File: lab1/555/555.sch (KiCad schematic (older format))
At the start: 8 parts, among them IC1 MC9S08QG8xPBE, U1 LM555

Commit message: actualizacion esquematico correccion tierra en LED-RGB e imagenes para el informe
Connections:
- net +5V: now also Rc.1
- net GND: no longer Rc.2
- net at D1.1 (A): now also Rc.2; no longer Rc.1
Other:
- moved on the sheet: Rc
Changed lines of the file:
@@
 $EndComp
-$Comp
-L power:GND #PWR?
-U 1 1 5EB46ACA
-P 6350 2050
-F 0 "#PWR?" H 6350 1800 50  0001 C CNN
-F 1 "GND" H 6355 1877 50  0000 C CNN
-F 2 "" H 6350 2050 50  0001 C CNN
-F 3 "" H 6350 2050 50  0001 C CNN
-	1    6350 2050
-	1    0    0    -1
-$EndComp
-Wire Wire Line
-	6350 1900 6350 2050
 $Comp
 L Device:R Rc
 U 1 1 5EB46152
-P 6350 1750
-F 0 "Rc" H 6420 1796 50  0000 L CNN
-F 1 "330" H 6420 1705 50  0000 L CNN
-F 2 "" V 6280 1750 50  0001 C CNN
-F 3 "~" H 6350 1750 50  0001 C CNN
-	1    6350 1750
+P 6350 1450
+F 0 "Rc" H 6420 1496 50  0000 L CNN
+F 1 "330" H 6420 1405 50  0000 L CNN
+F 2 "" V 6280 1450 50  0001 C CNN
+F 3 "~" H 6350 1450 50  0001 C CNN
+	1    6350 1450
 	1    0    0    -1
 $EndComp
@@
 	1    0    0    -1
 $EndComp
+$Comp
+L power:+5V #PWR?
+U 1 1 5EB49A53
+P 6350 1300
+F 0 "#PWR?" H 6350 1150 50  0001 C CNN
+F 1 "+5V" H 6365 1473 50  0000 C CNN
+F 2 "" H 6350 1300 50  0001 C CNN
+F 3 "" H 6350 1300 50  0001 C CNN
+	1    6350 1300
+	1    0    0    -1
+$EndComp

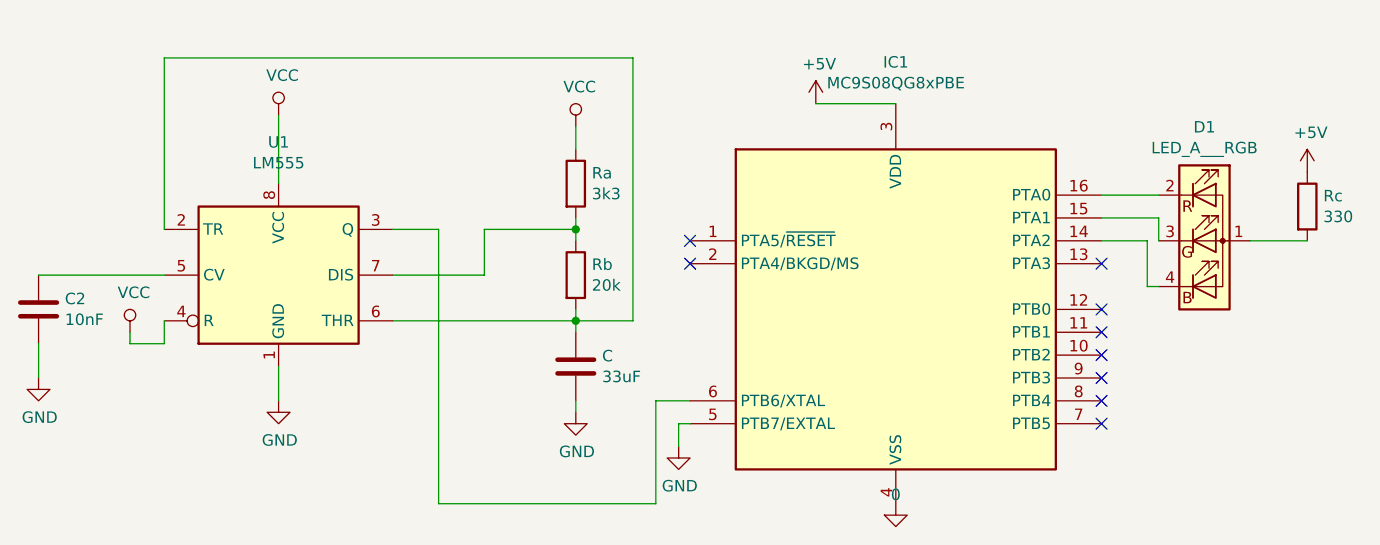
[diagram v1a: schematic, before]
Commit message: se actualizo en lab1 las fuentes de poder a 3v3, imagenes y esquematico
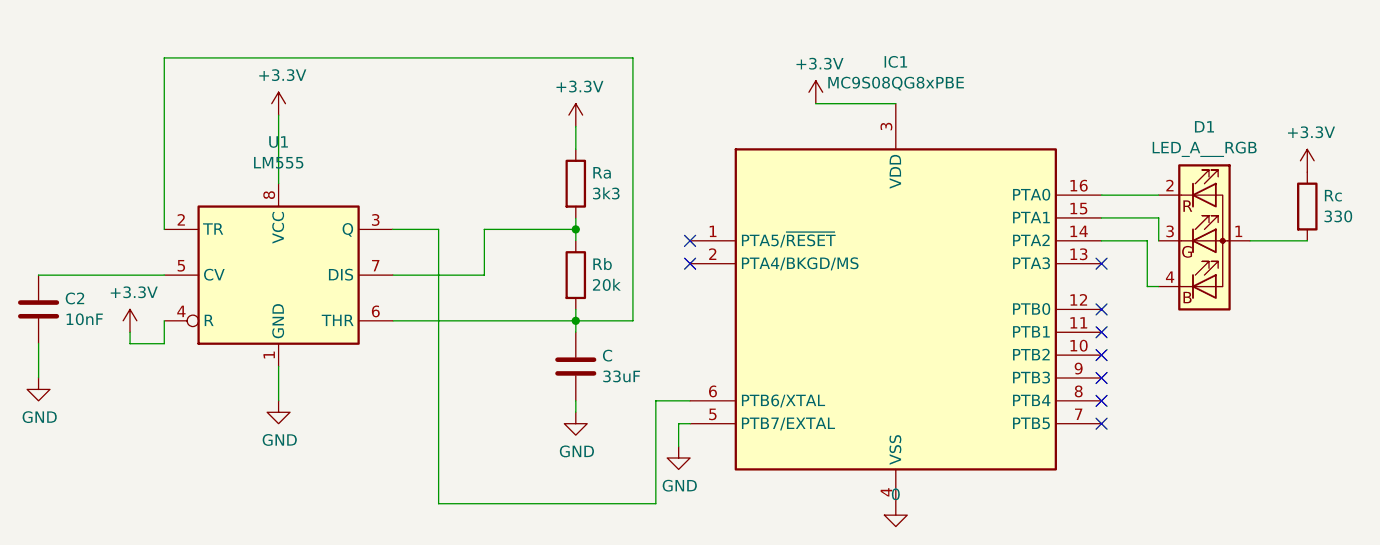
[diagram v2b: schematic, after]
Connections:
- net VCC is gone; now on net +3V3: Ra.1, U1.4 (R), U1.8 (VCC)
- net +5V renamed +3V3
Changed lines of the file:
@@
-	1    0    0    -1
-$EndComp
-$Comp
-L power:VCC #PWR?
-U 1 1 5EA5C293
-P 1850 1050
-F 0 "#PWR?" H 1850 900 50  0001 C CNN
-F 1 "VCC" H 1867 1223 50  0000 C CNN
-F 2 "" H 1850 1050 50  0001 C CNN
-F 3 "" H 1850 1050 50  0001 C CNN
-	1    1850 1050
-	1    0    0    -1
-$EndComp
-$Comp
-L power:VCC #PWR?
-U 1 1 5EA5C920
-P 1200 2000
-F 0 "#PWR?" H 1200 1850 50  0001 C CNN
-F 1 "VCC" H 1217 2173 50  0000 C CNN
-F 2 "" H 1200 2000 50  0001 C CNN
-F 3 "" H 1200 2000 50  0001 C CNN
-	1    1200 2000
 	1    0    0    -1
 $EndComp
@@
 	3150 1950 3150 2000
 Wire Wire Line
-	800  1750 1350 1750
-Wire Wire Line
 	800  2050 800  2200
 Wire Wire Line
@@
 Wire Wire Line
 	1350 800  3400 800
-$Comp
-L power:VCC #PWR?
-U 1 1 5EA68E96
-P 3150 1100
-F 0 "#PWR?" H 3150 950 50  0001 C CNN
-F 1 "VCC" H 3167 1273 50  0000 C CNN
-F 2 "" H 3150 1100 50  0001 C CNN
-F 3 "" H 3150 1100 50  0001 C CNN
-	1    3150 1100
-	1    0    0    -1
-$EndComp
 Wire Wire Line
 	3150 1100 3150 1200
@@
 Wire Wire Line
 	4550 1000 4200 1000
-$Comp
-L power:+5V #PWR?
-U 1 1 5EB36E31
-P 4200 1000
-F 0 "#PWR?" H 4200 850 50  0001 C CNN
-F 1 "+5V" H 4215 1173 50  0000 C CNN
-F 2 "" H 4200 1000 50  0001 C CNN
-F 3 "" H 4200 1000 50  0001 C CNN
-	1    4200 1000
-	1    0    0    -1
-$EndComp
 $Comp
 L pspice:0 #GND?
@@
 $EndComp
 $Comp
-L power:+5V #PWR?
-U 1 1 5EB49A53
+L power:+3.3V #PWR?
+U 1 1 5EC09E83
+P 4200 1000
+F 0 "#PWR?" H 4200 850 50  0001 C CNN
+F 1 "+3.3V" H 4215 1173 50  0000 C CNN
+F 2 "" H 4200 1000 50  0001 C CNN
+F 3 "" H 4200 1000 50  0001 C CNN
+	1    4200 1000
+	1    0    0    -1
+$EndComp
+$Comp
+L power:+3.3V #PWR?
+U 1 1 5EC0A9BE
 P 6350 1300
 F 0 "#PWR?" H 6350 1150 50  0001 C CNN
-F 1 "+5V" H 6365 1473 50  0000 C CNN
+F 1 "+3.3V" H 6365 1473 50  0000 C CNN
 F 2 "" H 6350 1300 50  0001 C CNN
 F 3 "" H 6350 1300 50  0001 C CNN
@@
 	1    0    0    -1
 $EndComp
+$Comp
+L power:+3.3V #PWR?
+U 1 1 5EC0DF4A
+P 3150 1100
+F 0 "#PWR?" H 3150 950 50  0001 C CNN
+F 1 "+3.3V" H 3165 1273 50  0000 C CNN
+F 2 "" H 3150 1100 50  0001 C CNN
+F 3 "" H 3150 1100 50  0001 C CNN
+	1    3150 1100
+	1    0    0    -1
+$EndComp
+$Comp
+L power:+3.3V #PWR?
+U 1 1 5EC0E7E2
+P 1850 1050
+F 0 "#PWR?" H 1850 900 50  0001 C CNN
+F 1 "+3.3V" H 1865 1223 50  0000 C CNN
+F 2 "" H 1850 1050 50  0001 C CNN
+F 3 "" H 1850 1050 50  0001 C CNN
+	1    1850 1050
+	1    0    0    -1
+$EndComp
+$Comp
+L power:+3.3V #PWR?
+U 1 1 5EC0EFC0
+P 1200 2000
+F 0 "#PWR?" H 1200 1850 50  0001 C CNN
+F 1 "+3.3V" H 1215 2173 50  0000 C CNN
+F 2 "" H 1200 2000 50  0001 C CNN
+F 3 "" H 1200 2000 50  0001 C CNN
+	1    1200 2000
+	1    0    0    -1
+$EndComp
+Wire Wire Line
+	1350 1750 800  1750
 $EndSCHEMATC

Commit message: agregados condensadores entre VCC y Vdd al esquematico
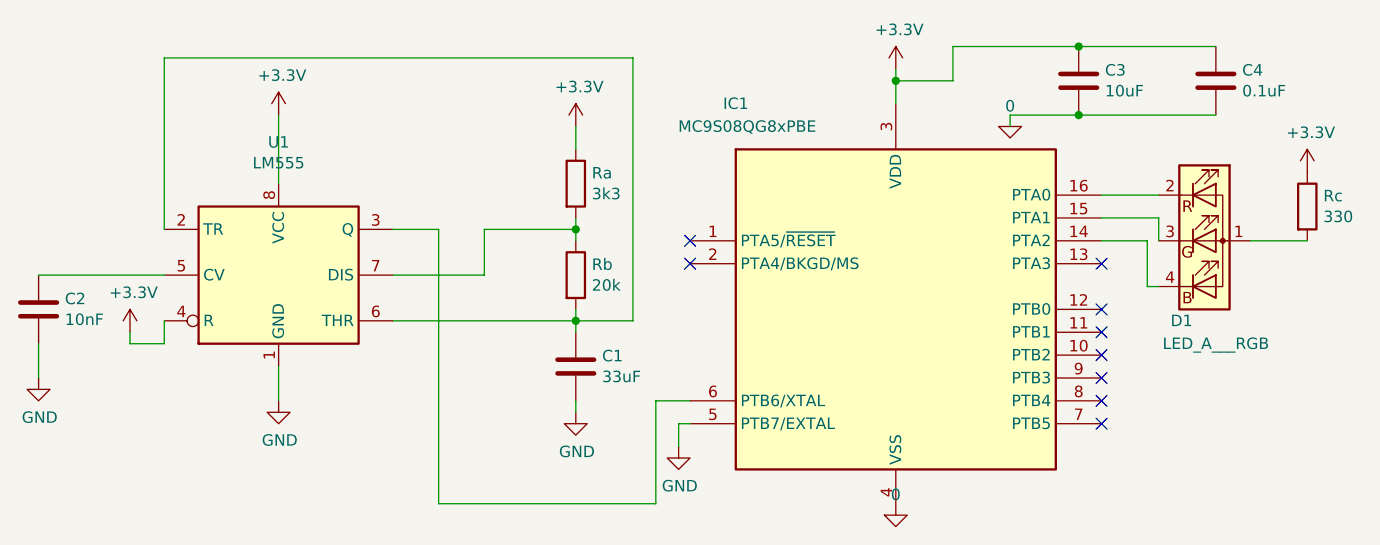
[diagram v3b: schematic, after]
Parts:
- added C3: 10uF, symbol Device:C
- added C4: 0.1uF, symbol Device:C
- renumbered C to C1
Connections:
- net +3V3: now also C3.1, C4.1
- net 0: now also C3.2, C4.2
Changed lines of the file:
@@
 $EndDescr
 $Comp
-L Device:C C
+L Device:C C1
 U 1 1 5EA59322
 P 3150 2150
-F 0 "C" H 3265 2196 50  0000 L CNN
+F 0 "C1" H 3265 2196 50  0000 L CNN
 F 1 "33uF" H 3265 2105 50  0000 L CNN
 F 2 "" H 3188 2000 50  0001 C CNN
@@
 Wire Wire Line
 	1850 2150 1850 2300
-Wire Wire Line
-	4550 1000 4200 1000
 $Comp
 L pspice:0 #GND?
@@
 	1    0    0    -1
 $EndComp
-$Comp
-L Device:LED_ARGB D1
-U 1 1 5EB43DE4
-P 5900 1600
-F 0 "D1" H 5900 2097 50  0000 C CNN
-F 1 "LED_A___RGB" H 5900 2006 50  0000 C CNN
-F 2 "" H 5900 1550 50  0001 C CNN
-F 3 "~" H 5900 1550 50  0001 C CNN
-	1    5900 1600
-	1    0    0    -1
-$EndComp
+Wire Wire Line
+	2550 1550 2550 2750
+Wire Wire Line
+	2550 2750 3500 2750
+Wire Wire Line
+	3500 2750 3500 2300
+$Comp
+L power:GND #PWR?
+U 1 1 5EB4FC4B
+P 3600 2500
+F 0 "#PWR?" H 3600 2250 50  0001 C CNN
+F 1 "GND" H 3605 2327 50  0000 C CNN
+F 2 "" H 3600 2500 50  0001 C CNN
+F 3 "" H 3600 2500 50  0001 C CNN
+	1    3600 2500
+	1    0    0    -1
+$EndComp
+Wire Wire Line
+	3650 2400 3600 2400
+Wire Wire Line
+	3600 2400 3600 2500
+NoConn ~ 5450 2200
+NoConn ~ 5450 2300
+NoConn ~ 5450 2400
+NoConn ~ 3650 1700
+NoConn ~ 3650 1600
+Wire Wire Line
+	3400 1950 3150 1950
+Wire Wire Line
+	3500 2300 3650 2300
+NoConn ~ 5450 2100
+NoConn ~ 5450 2000
+NoConn ~ 5450 1900
+NoConn ~ 5450 1700
+$Comp
+L MCU_NXP_S08:MC9S08QG8xPBE IC1
+U 1 1 5EB35528
+P 4550 1900
+F 0 "IC1" H 3850 2800 50  0000 C CNN
+F 1 "MC9S08QG8xPBE" H 3900 2700 50  0000 C CNN
+F 2 "Package_DIP:DIP-16_W7.62mm" H 4750 1150 50  0001 L CIN
+F 3 "http://cache.nxp.com/files/microcontrollers/doc/data_sheet/MC9S08QG8.pdf" H 4650 1700 50  0001 C CNN
+	1    4550 1900
+	1    0    0    -1
+$EndComp
+Wire Wire Line
+	2350 1950 3150 1950
+Wire Wire Line
+	2350 1750 2750 1750
+Wire Wire Line
+	2350 1550 2550 1550
+$Comp
+L Timer:LM555 U1
+U 1 1 5EA5A9CA
+P 1850 1750
+F 0 "U1" H 1850 2331 50  0000 C CNN
+F 1 "LM555" H 1850 2240 50  0000 C CNN
+F 2 "" H 1850 1750 50  0001 C CNN
+F 3 "http://www.ti.com/lit/ds/symlink/lm555.pdf" H 1850 1750 50  0001 C CNN
+	1    1850 1750
+	1    0    0    -1
+$EndComp
+$Comp
+L power:+3.3V #PWR?
+U 1 1 5EC09E83
+P 4550 850
+F 0 "#PWR?" H 4550 700 50  0001 C CNN
+F 1 "+3.3V" H 4565 1023 50  0000 C CNN
+F 2 "" H 4550 850 50  0001 C CNN
+F 3 "" H 4550 850 50  0001 C CNN
+	1    4550 850
+	1    0    0    -1
+$EndComp
+$Comp
+L power:+3.3V #PWR?
+U 1 1 5EC0DF4A
+P 3150 1100
+F 0 "#PWR?" H 3150 950 50  0001 C CNN
+F 1 "+3.3V" H 3165 1273 50  0000 C CNN
+F 2 "" H 3150 1100 50  0001 C CNN
+F 3 "" H 3150 1100 50  0001 C CNN
+	1    3150 1100
+	1    0    0    -1
+$EndComp
+$Comp
+L power:+3.3V #PWR?
+U 1 1 5EC0E7E2
+P 1850 1050
+F 0 "#PWR?" H 1850 900 50  0001 C CNN
+F 1 "+3.3V" H 1865 1223 50  0000 C CNN
+F 2 "" H 1850 1050 50  0001 C CNN
+F 3 "" H 1850 1050 50  0001 C CNN
+	1    1850 1050
+	1    0    0    -1
+$EndComp
+$Comp
+L power:+3.3V #PWR?
+U 1 1 5EC0EFC0
+P 1200 2000
+F 0 "#PWR?" H 1200 1850 50  0001 C CNN
+F 1 "+3.3V" H 1215 2173 50  0000 C CNN
+F 2 "" H 1200 2000 50  0001 C CNN
+F 3 "" H 1200 2000 50  0001 C CNN
+	1    1200 2000
+	1    0    0    -1
+$EndComp
+Wire Wire Line
+	1350 1750 800  1750
+$Comp
+L Device:C C4
+U 1 1 5EC0DAD6
+P 5950 900
+F 0 "C4" H 6065 946 50  0000 L CNN
+F 1 "0.1uF" H 6065 855 50  0000 L CNN
+F 2 "" H 5988 750 50  0001 C CNN
+F 3 "~" H 5950 900 50  0001 C CNN
+	1    5950 900
+	1    0    0    -1
+$EndComp
+$Comp
+L Device:C C3
+U 1 1 5EC0E77D
+P 5350 900
+F 0 "C3" H 5465 946 50  0000 L CNN
+F 1 "10uF" H 5465 855 50  0000 L CNN
+F 2 "" H 5388 750 50  0001 C CNN
+F 3 "~" H 5350 900 50  0001 C CNN
+	1    5350 900
+	1    0    0    -1
+$EndComp
+Connection ~ 5350 750
+Connection ~ 5350 1050
+Wire Wire Line
+	5350 750  5950 750
+Wire Wire Line
+	5350 1050 5950 1050
+Wire Wire Line
+	4800 750  4800 900
+Wire Wire Line
+	4800 900  4550 900
+Wire Wire Line
+	4550 900  4550 1000
+Wire Wire Line
+	4800 750  5350 750
+Wire Wire Line
+	4550 850  4550 900
+Connection ~ 4550 900
+$Comp
+L pspice:0 #GND?
+U 1 1 5EC1583C
+P 5050 1100
+F 0 "#GND?" H 5050 1000 50  0001 C CNN
+F 1 "0" H 5050 1189 50  0000 C CNN
+F 2 "" H 5050 1100 50  0001 C CNN
+F 3 "~" H 5050 1100 50  0001 C CNN
+	1    5050 1100
+	1    0    0    -1
+$EndComp
+Wire Wire Line
+	5050 1050 5050 1100
+Wire Wire Line
+	5050 1050 5350 1050
+$Comp
+L power:+3.3V #PWR?
+U 1 1 5EC0A9BE
+P 6350 1300
+F 0 "#PWR?" H 6350 1150 50  0001 C CNN
+F 1 "+3.3V" H 6365 1473 50  0000 C CNN
+F 2 "" H 6350 1300 50  0001 C CNN
+F 3 "" H 6350 1300 50  0001 C CNN
+	1    6350 1300
+	1    0    0    -1
+$EndComp
+Wire Wire Line
+	5650 1800 5700 1800
+Wire Wire Line
+	5650 1600 5650 1800
+Wire Wire Line
+	5450 1600 5650 1600
+Wire Wire Line
+	5700 1500 5700 1600
+Wire Wire Line
+	5450 1500 5700 1500
+Wire Wire Line
+	5450 1400 5700 1400
+Wire Wire Line
+	6100 1600 6350 1600
 $Comp
 L Device:R Rc
@@
 	1    0    0    -1
 $EndComp
-Wire Wire Line
-	6100 1600 6350 1600
-Wire Wire Line
-	2550 1550 2550 2750
-Wire Wire Line
-	2550 2750 3500 2750
-Wire Wire Line
-	3500 2750 3500 2300
-$Comp
-L power:GND #PWR?
-U 1 1 5EB4FC4B
-P 3600 2500
-F 0 "#PWR?" H 3600 2250 50  0001 C CNN
-F 1 "GND" H 3605 2327 50  0000 C CNN
-F 2 "" H 3600 2500 50  0001 C CNN
-F 3 "" H 3600 2500 50  0001 C CNN
-	1    3600 2500
-	1    0    0    -1
-$EndComp
-Wire Wire Line
-	3650 2400 3600 2400
-Wire Wire Line
-	3600 2400 3600 2500
-NoConn ~ 5450 2200
-NoConn ~ 5450 2300
-NoConn ~ 5450 2400
-NoConn ~ 3650 1700
-NoConn ~ 3650 1600
-Wire Wire Line
-	3400 1950 3150 1950
-Wire Wire Line
-	3500 2300 3650 2300
-NoConn ~ 5450 2100
-NoConn ~ 5450 2000
-NoConn ~ 5450 1900
-NoConn ~ 5450 1700
-Wire Wire Line
-	5450 1400 5700 1400
-Wire Wire Line
-	5450 1500 5700 1500
-Wire Wire Line
-	5700 1500 5700 1600
-Wire Wire Line
-	5450 1600 5650 1600
-Wire Wire Line
-	5650 1600 5650 1800
-Wire Wire Line
-	5650 1800 5700 1800
-$Comp
-L MCU_NXP_S08:MC9S08QG8xPBE IC1
-U 1 1 5EB35528
-P 4550 1900
-F 0 "IC1" H 4550 2981 50  0000 C CNN
-F 1 "MC9S08QG8xPBE" H 4550 2890 50  0000 C CNN
-F 2 "Package_DIP:DIP-16_W7.62mm" H 4750 1150 50  0001 L CIN
-F 3 "http://cache.nxp.com/files/microcontrollers/doc/data_sheet/MC9S08QG8.pdf" H 4650 1700 50  0001 C CNN
-	1    4550 1900
-	1    0    0    -1
-$EndComp
-Wire Wire Line
-	2350 1950 3150 1950
-Wire Wire Line
-	2350 1750 2750 1750
-Wire Wire Line
-	2350 1550 2550 1550
-$Comp
-L Timer:LM555 U1
-U 1 1 5EA5A9CA
-P 1850 1750
-F 0 "U1" H 1850 2331 50  0000 C CNN
-F 1 "LM555" H 1850 2240 50  0000 C CNN
-F 2 "" H 1850 1750 50  0001 C CNN
-F 3 "http://www.ti.com/lit/ds/symlink/lm555.pdf" H 1850 1750 50  0001 C CNN
-	1    1850 1750
-	1    0    0    -1
-$EndComp
-$Comp
-L power:+3.3V #PWR?
-U 1 1 5EC09E83
-P 4200 1000
-F 0 "#PWR?" H 4200 850 50  0001 C CNN
-F 1 "+3.3V" H 4215 1173 50  0000 C CNN
-F 2 "" H 4200 1000 50  0001 C CNN
-F 3 "" H 4200 1000 50  0001 C CNN
-	1    4200 1000
-	1    0    0    -1
-$EndComp
-$Comp
-L power:+3.3V #PWR?
-U 1 1 5EC0A9BE
-P 6350 1300
-F 0 "#PWR?" H 6350 1150 50  0001 C CNN
-F 1 "+3.3V" H 6365 1473 50  0000 C CNN
-F 2 "" H 6350 1300 50  0001 C CNN
-F 3 "" H 6350 1300 50  0001 C CNN
-	1    6350 1300
-	1    0    0    -1
-$EndComp
-$Comp
-L power:+3.3V #PWR?
-U 1 1 5EC0DF4A
-P 3150 1100
-F 0 "#PWR?" H 3150 950 50  0001 C CNN
-F 1 "+3.3V" H 3165 1273 50  0000 C CNN
-F 2 "" H 3150 1100 50  0001 C CNN
-F 3 "" H 3150 1100 50  0001 C CNN
-	1    3150 1100
-	1    0    0    -1
-$EndComp
-$Comp
-L power:+3.3V #PWR?
-U 1 1 5EC0E7E2
-P 1850 1050
-F 0 "#PWR?" H 1850 900 50  0001 C CNN
-F 1 "+3.3V" H 1865 1223 50  0000 C CNN
-F 2 "" H 1850 1050 50  0001 C CNN
-F 3 "" H 1850 1050 50  0001 C CNN
-	1    1850 1050
-	1    0    0    -1
-$EndComp
-$Comp
-L power:+3.3V #PWR?
-U 1 1 5EC0EFC0
-P 1200 2000
-F 0 "#PWR?" H 1200 1850 50  0001 C CNN
-F 1 "+3.3V" H 1215 2173 50  0000 C CNN
-F 2 "" H 1200 2000 50  0001 C CNN
-F 3 "" H 1200 2000 50  0001 C CNN
-	1    1200 2000
-	1    0    0    -1
-$EndComp
-Wire Wire Line
-	1350 1750 800  1750
+$Comp
+L Device:LED_ARGB D1
+U 1 1 5EB43DE4
+P 5900 1600
+F 0 "D1" H 5800 1250 50  0000 C CNN
+F 1 "LED_A___RGB" H 5950 1150 50  0000 C CNN
+F 2 "" H 5900 1550 50  0001 C CNN
+F 3 "~" H 5900 1550 50  0001 C CNN
+	1    5900 1600
+	1    0    0    -1
+$EndComp
 $EndSCHEMATC
